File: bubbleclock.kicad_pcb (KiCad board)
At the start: 2 copper layers, 22.9 x 57.2 mm, 34 parts, among them J1 Conn_01x01_Male, J2 Conn_01x01_Male, J3 Conn_01x05_Male, J4 14_seg_bubbledisp, Q1 Q_NPN_BEC, Q2 Q_NPN_BEC, SW1 SW_SPDT, U1 ESP-12F, U2 MIC5504-3.3YM5, U3 74HC595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

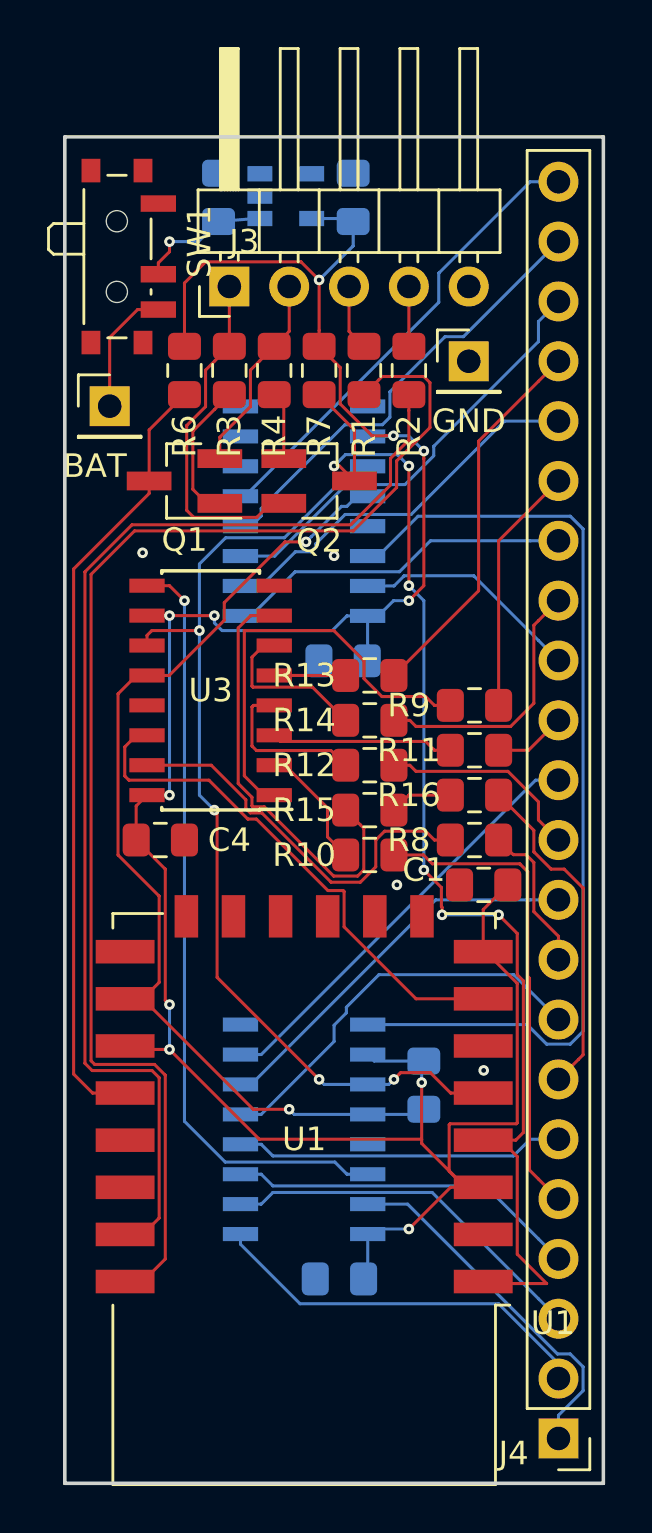
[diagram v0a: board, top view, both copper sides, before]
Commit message: Redesigned with looser tolerances
Don't torture the boardhouse, plus implementing schematic fixes

Fixes:
1. Pull GPIO0 low instead of high
2. Short regulator enable to VIN
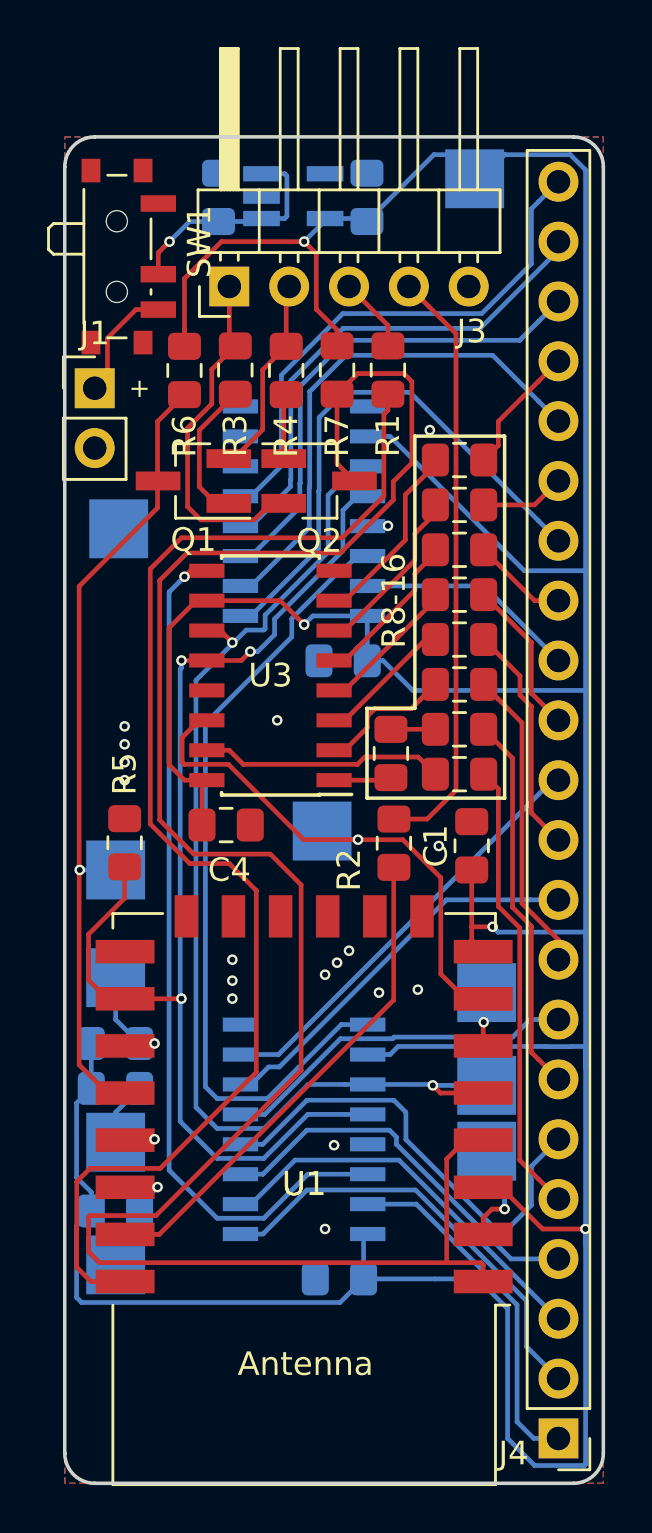
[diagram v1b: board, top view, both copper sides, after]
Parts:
- removed J2: Conn_01x01_Male, Connector_PinHeader_2.54mm:PinHeader_1x01_P2.54mm_Vertical
- added R17: 10K, Resistor_SMD:R_0805_2012Metric_Pad1.15x1.40mm_HandSolder, B.Cu at (202.2, 103.9)
- added R18: 10K, Resistor_SMD:R_0805_2012Metric_Pad1.15x1.40mm_HandSolder, B.Cu at (202.2, 105.8)
- added R19: 10K, Resistor_SMD:R_0805_2012Metric_Pad1.15x1.40mm_HandSolder, B.Cu at (202.2, 111.0)
- added TP1: TestPoint, TestPoint:TestPoint_Pad_2.5x2.5mm, B.Cu at (217.4, 67.2)
- added TP10: TestPoint, TestPoint:TestPoint_Pad_2.5x2.5mm, B.Cu at (217.9, 105.7)
- added TP2: TestPoint, TestPoint:TestPoint_Pad_2.5x2.5mm, B.Cu at (217.9, 101.7)
- added TP3: TestPoint, TestPoint:TestPoint_Pad_2.5x2.5mm, B.Cu at (202.2, 108.1)
- added TP4: TestPoint, TestPoint:TestPoint_Pad_2.5x2.5mm, B.Cu at (202.2, 96.5)
- added TP5: TestPoint, TestPoint:TestPoint_Pad_2.5x2.5mm, B.Cu at (202.3, 82.0)
- added TP6: TestPoint, TestPoint:TestPoint_Pad_2.5x2.5mm, B.Cu at (210.9, 94.9)
- added TP7: TestPoint, TestPoint:TestPoint_Pad_2.5x2.5mm, B.Cu at (202.2, 113.3)
- added TP8: TestPoint, TestPoint:TestPoint_Pad_2.5x2.5mm, B.Cu at (202.2, 101.1)
- added TP9: TestPoint, TestPoint:TestPoint_Pad_2.5x2.5mm, B.Cu at (217.9, 108.5)
- J1: value Conn_01x01_Male -> Conn_01x02_Male; footprint Connector_PinHeader_2.54mm:PinHeader_1x01_P2.54mm_Vertical -> Connector_PinHeader_2.54mm:PinHeader_1x02_P2.54mm_Vertical
- R5: moved to F.Cu
- U2: footprint Package_TO_SOT_SMD:SOT-23-5 -> Package_TO_SOT_SMD:SOT-23-5_HandSoldering
- moved R2 20.1 mm to (214.0, 95.4)
- moved R5 16.3 mm to (202.6, 95.4), turned to 90 degrees
- moved R13 9.91 mm to (216.8, 79.1)
- moved R9 8.53 mm to (216.8, 81.0)
- moved R14 8.18 mm to (216.8, 82.9)
- moved R11 6.63 mm to (216.8, 84.8)
- moved R8 6.63 mm to (216.8, 88.6)
- moved R12 6.55 mm to (216.8, 86.7)
- moved R10 5.13 mm to (216.8, 92.5)
- moved R16 2.87 mm to (216.8, 90.6)
- moved C4 2.87 mm to (206.9, 94.6)
- moved U3 2.62 mm to (208.8, 88.3)
- moved R15 2.57 mm to (213.9, 91.6), turned to 270 degrees
- moved C1 1.74 mm to (217.3, 95.5), turned to 90 degrees
- moved R1 1.02 mm to (213.7, 75.3)
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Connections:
- net Net-(J4-Pad1) renamed /C1
- net Net-(J4-Pad10) renamed /C7
- net Net-(J4-Pad11) renamed /AE'
- net Net-(J4-Pad12) renamed /C8
- net Net-(J4-Pad13) renamed /AD'
- net Net-(J4-Pad14) renamed /C9
- net Net-(J4-Pad15) renamed /AG'
- net Net-(J4-Pad16) renamed /C10
- net Net-(J4-Pad17) renamed /AB'
- net Net-(J4-Pad18) renamed /C11
- net Net-(J4-Pad19) renamed /AF'
- net Net-(J4-Pad2) renamed /C2
- net Net-(J4-Pad20) renamed /C12
- net Net-(J4-Pad21) renamed /C13
- net Net-(J4-Pad22) renamed /C14
- net Net-(J4-Pad3) renamed /C3
- net Net-(J4-Pad4) renamed /C4
- net Net-(J4-Pad5) renamed /AC'
- net Net-(J4-Pad6) renamed /C5
- net Net-(J4-Pad7) renamed /ADP'
- net Net-(J4-Pad8) renamed /C6
- net Net-(J4-Pad9) renamed /AA'
- net Net-(Q1-Pad1) renamed /RTS'
- net Net-(Q2-Pad1) renamed /DTR'
- net Net-(U3-Pad9) renamed /CHAIN1
- net Net-(U4-Pad9) renamed /CHAIN2
- R5 pad 1: +3V3 -> /CS
- R5 pad 2: /CS -> GND
- U1 pad 10: Net-(U1-Pad10) -> (no net)
- U1 pad 11: Net-(U1-Pad11) -> (no net)
- U1 pad 12: Net-(U1-Pad12) -> (no net)
- U1 pad 13: Net-(U1-Pad13) -> (no net)
- U1 pad 14: Net-(U1-Pad14) -> (no net)
- U1 pad 17: +3V3 -> /GPIO2
- U1 pad 19: GND -> /SDA
- U1 pad 2: Net-(U1-Pad2) -> /ADC
- U1 pad 20: GND -> /SCL
- U1 pad 6: GND -> /MISO
- U1 pad 9: Net-(U1-Pad9) -> (no net)
- U2 pad 3: Net-(U2-Pad3) -> Net-(C2-Pad1)
- U2 pad 4: Net-(U2-Pad4) -> (no net)
- U3 pad 1: /AB -> /ADP
- U3 pad 15: /AA -> /AC
- U3 pad 2: /AC -> /AA
- U3 pad 3: /AD -> /AE
- U3 pad 4: /AE -> /AD
- U3 pad 5: /AF -> /AG
- U3 pad 6: /AG -> /AB
- U3 pad 7: /ADP -> /AF
- U5 pad 6: Net-(U5-Pad6) -> (no net)
- U5 pad 7: Net-(U5-Pad7) -> (no net)
- U5 pad 9: Net-(U5-Pad9) -> (no net)
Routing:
- net +3V3: track 116.0 -> 193.9 mm, vias 11 -> 4
- net /RESET: track 52.9 -> 86.6 mm, vias 6 -> 0
- net /RXD: track 50.6 -> 20.7 mm
- net Net-(J3-Pad4): track 2.54 -> 25.4 mm
- net /ADP: track 18.5 -> 2.46 mm
- net /AA: track 16.9 -> 5.74 mm
- net /AB: track 18.3 -> 7.38 mm
- net /AF': track 16.2 -> 5.51 mm
- net /C10: track 14.8 -> 23.3 mm
- net /CS: track 43.3 -> 50.9 mm, vias 2 -> 3
- net /CHAIN2: track 41.1 -> 34.1 mm
- net /AB': track 10.6 -> 3.60 mm
- net /AG': track 11.2 -> 4.32 mm
- net /AA': track 6.45 -> 13.0 mm
- net /SDA: track 0.00 -> 5.68 mm, vias 0 -> 1
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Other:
- outline, holes or cut-outs redrawn
- net class Default: clearance 0.13 -> 0.2; trace_width 0.13 -> 0.2; via_drill 0.2 -> 0.25
- rule trace_clearance: 0.13 -> 0.2
- rule trace_min: 0.13 -> 0.2
- rule via_min_drill: 0.2 -> 0.25
- board text added: "+"
- board text added: "+3V3"
- board text added: "ADC"
- board text added: "GPIO0"
- board text added: "GPIO2"
- board text added: "MISO"
- board text added: "MOSI"
- board text added: "R8-16"
- board text added: "SCK"
- board text added: "SCL"
- board text added: "SDA"
- board text removed: "BAT"
